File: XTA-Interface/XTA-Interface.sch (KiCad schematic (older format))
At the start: 17 parts, among them CN1 DRIVE 0, CN2 DRIVE 1, CN3 LEDs, CN4 Drive Power, J3 Bus_ISA_8bit, U1 BIOS FLASH, U2 74HCT245, U3 ATF/GAL16V8-15 \"LEFT\", U4 ATF/GAL16V8-15 \"RIGHT\"

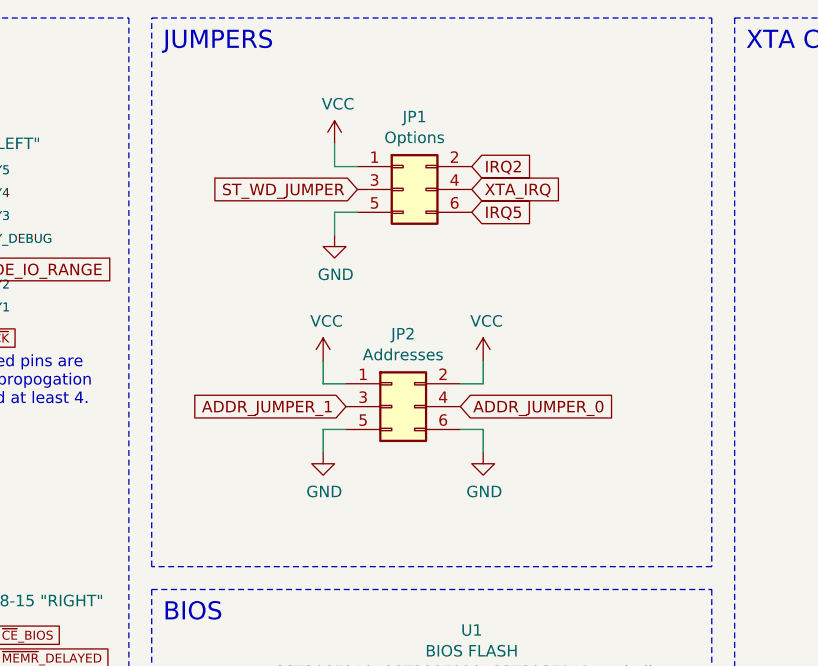
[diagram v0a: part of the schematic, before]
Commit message: Swap positions of A and B jumpers.
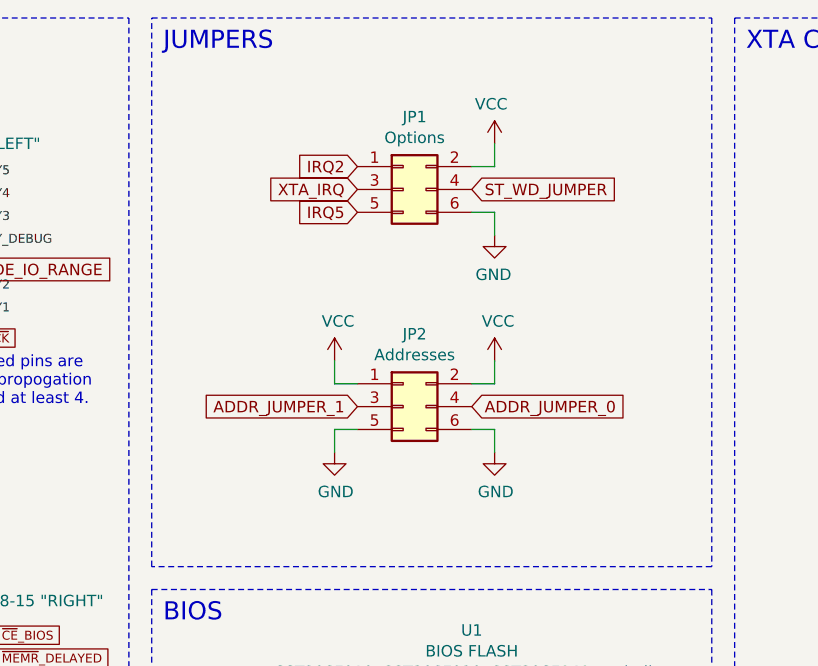
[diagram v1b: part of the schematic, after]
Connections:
- net GND: now also JP1.6 (Pin_6); no longer JP1.5 (Pin_5)
- net IRQ2: now also JP1.1 (Pin_1); no longer JP1.2 (Pin_2)
- net IRQ5: now also JP1.5 (Pin_5); no longer JP1.6 (Pin_6)
- net ST_WD_JUMPER: now also JP1.4 (Pin_4); no longer JP1.3 (Pin_3)
- net VCC: now also JP1.2 (Pin_2); no longer JP1.1 (Pin_1)
- net XTA_IRQ: now also JP1.3 (Pin_3); no longer JP1.4 (Pin_4)
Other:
- moved on the sheet: JP2
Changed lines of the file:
@@
 L power:VCC #PWR0104
 U 1 1 60CA784E
-P 6650 2050
-F 0 "#PWR0104" H 6650 1900 50  0001 C CNN
-F 1 "VCC" H 6665 2223 50  0000 C CNN
-F 2 "" H 6650 2050 50  0001 C CNN
-F 3 "" H 6650 2050 50  0001 C CNN
-	1    6650 2050
+P 6700 2050
+F 0 "#PWR0104" H 6700 1900 50  0001 C CNN
+F 1 "VCC" H 6715 2223 50  0000 C CNN
+F 2 "" H 6700 2050 50  0001 C CNN
+F 3 "" H 6700 2050 50  0001 C CNN
+	1    6700 2050
 	1    0    0    -1
 $EndComp
@@
 L power:VCC #PWR0114
 U 1 1 60CA7D3F
-P 7350 2050
-F 0 "#PWR0114" H 7350 1900 50  0001 C CNN
-F 1 "VCC" H 7365 2223 50  0000 C CNN
-F 2 "" H 7350 2050 50  0001 C CNN
-F 3 "" H 7350 2050 50  0001 C CNN
-	1    7350 2050
+P 7400 2050
+F 0 "#PWR0114" H 7400 1900 50  0001 C CNN
+F 1 "VCC" H 7415 2223 50  0000 C CNN
+F 2 "" H 7400 2050 50  0001 C CNN
+F 3 "" H 7400 2050 50  0001 C CNN
+	1    7400 2050
 	1    0    0    -1
 $EndComp
@@
 L power:GND #PWR0135
 U 1 1 60CA7F88
-P 6650 2450
-F 0 "#PWR0135" H 6650 2200 50  0001 C CNN
-F 1 "GND" H 6655 2277 50  0000 C CNN
-F 2 "" H 6650 2450 50  0001 C CNN
-F 3 "" H 6650 2450 50  0001 C CNN
-	1    6650 2450
+P 6700 2450
+F 0 "#PWR0135" H 6700 2200 50  0001 C CNN
+F 1 "GND" H 6705 2277 50  0000 C CNN
+F 2 "" H 6700 2450 50  0001 C CNN
+F 3 "" H 6700 2450 50  0001 C CNN
+	1    6700 2450
 	1    0    0    -1
 $EndComp
@@
 L power:GND #PWR0136
 U 1 1 60CA8362
-P 7350 2450
-F 0 "#PWR0136" H 7350 2200 50  0001 C CNN
-F 1 "GND" H 7355 2277 50  0000 C CNN
-F 2 "" H 7350 2450 50  0001 C CNN
-F 3 "" H 7350 2450 50  0001 C CNN
-	1    7350 2450
-	1    0    0    -1
-$EndComp
-Wire Wire Line
-	6650 2050 6650 2150
-Wire Wire Line
-	6650 2150 6750 2150
-Wire Wire Line
-	6750 2350 6650 2350
-Wire Wire Line
-	6650 2350 6650 2450
-Wire Wire Line
-	7250 2350 7350 2350
-Wire Wire Line
-	7350 2350 7350 2450
-Wire Wire Line
-	7250 2150 7350 2150
-Wire Wire Line
-	7350 2150 7350 2050
-Text GLabel 7250 2250 2    50   Input ~ 0
+P 7400 2450
+F 0 "#PWR0136" H 7400 2200 50  0001 C CNN
+F 1 "GND" H 7405 2277 50  0000 C CNN
+F 2 "" H 7400 2450 50  0001 C CNN
+F 3 "" H 7400 2450 50  0001 C CNN
+	1    7400 2450
+	1    0    0    -1
+$EndComp
+Wire Wire Line
+	6700 2050 6700 2150
+Wire Wire Line
+	6700 2150 6800 2150
+Wire Wire Line
+	6800 2350 6700 2350
+Wire Wire Line
+	6700 2350 6700 2450
+Wire Wire Line
+	7300 2350 7400 2350
+Wire Wire Line
+	7400 2350 7400 2450
+Wire Wire Line
+	7300 2150 7400 2150
+Wire Wire Line
+	7400 2150 7400 2050
+Text GLabel 7300 2250 2    50   Input ~ 0
 ADDR_JUMPER_0
 $Comp
 L power:VCC #PWR0137
 U 1 1 60CBC833
-P 6700 1100
-F 0 "#PWR0137" H 6700 950 50  0001 C CNN
-F 1 "VCC" H 6715 1273 50  0000 C CNN
-F 2 "" H 6700 1100 50  0001 C CNN
-F 3 "" H 6700 1100 50  0001 C CNN
-	1    6700 1100
-	1    0    0    -1
+P 7400 1100
+F 0 "#PWR0137" H 7400 950 50  0001 C CNN
+F 1 "VCC" H 7415 1273 50  0000 C CNN
+F 2 "" H 7400 1100 50  0001 C CNN
+F 3 "" H 7400 1100 50  0001 C CNN
+	1    7400 1100
+	-1   0    0    -1
 $EndComp
 $Comp
 L power:GND #PWR0138
 U 1 1 60CBC847
-P 6700 1500
-F 0 "#PWR0138" H 6700 1250 50  0001 C CNN
-F 1 "GND" H 6705 1327 50  0000 C CNN
-F 2 "" H 6700 1500 50  0001 C CNN
-F 3 "" H 6700 1500 50  0001 C CNN
-	1    6700 1500
-	1    0    0    -1
-$EndComp
-Wire Wire Line
-	6700 1100 6700 1200
-Wire Wire Line
-	6700 1200 6800 1200
-Wire Wire Line
-	6800 1400 6700 1400
-Wire Wire Line
-	6700 1400 6700 1500
+P 7400 1500
+F 0 "#PWR0138" H 7400 1250 50  0001 C CNN
+F 1 "GND" H 7405 1327 50  0000 C CNN
+F 2 "" H 7400 1500 50  0001 C CNN
+F 3 "" H 7400 1500 50  0001 C CNN
+	1    7400 1500
+	-1   0    0    -1
+$EndComp
+Wire Wire Line
+	7400 1100 7400 1200
+Wire Wire Line
+	7400 1200 7300 1200
+Wire Wire Line
+	7300 1400 7400 1400
+Wire Wire Line
+	7400 1400 7400 1500
 Text GLabel 9450 2850 0    39   Input ~ 0
 ~DRV_ACTIVE
@@
 Text GLabel 9450 3900 0    50   Input ~ 0
 D7
-Text GLabel 6750 2250 0    50   Input ~ 0
+Text GLabel 6800 2250 0    50   Input ~ 0
 ADDR_JUMPER_1
+Text GLabel 7300 1300 2    50   Input ~ 0
+ST_WD_JUMPER
 Text GLabel 6800 1300 0    50   Input ~ 0
-ST_WD_JUMPER
-Text GLabel 7300 1300 2    50   Input ~ 0
 XTA_IRQ
 Text GLabel 1200 3200 0    50   Input ~ 0
@@
 Text GLabel 950  1300 0    50   Input ~ 0
 IRQ2
-Text GLabel 7300 1200 2    50   Input ~ 0
+Text GLabel 6800 1200 0    50   Input ~ 0
 IRQ2
-Text GLabel 7300 1400 2    50   Input ~ 0
+Text GLabel 6800 1400 0    50   Input ~ 0
 IRQ5
 $Comp
@@
 L Connector_Generic:Conn_02x03_Odd_Even JP2
 U 1 1 60CA67F2
-P 6950 2250
-F 0 "JP2" H 7000 2567 50  0000 C CNN
-F 1 "Addresses" H 7000 2476 50  0000 C CNN
-F 2 "Connector_PinHeader_2.54mm:PinHeader_2x03_P2.54mm_Vertical" H 6950 2250 50  0001 C CNN
-F 3 "~" H 6950 2250 50  0001 C CNN
-	1    6950 2250
-	1    0    0    -1
-$EndComp
+P 7000 2250
+F 0 "JP2" H 7050 2567 50  0000 C CNN
+F 1 "Addresses" H 7050 2476 50  0000 C CNN
+F 2 "Connector_PinHeader_2.54mm:PinHeader_2x03_P2.54mm_Vertical" H 7000 2250 50  0001 C CNN
+F 3 "~" H 7000 2250 50  0001 C CNN
+	1    7000 2250
+	1    0    0    -1
+$EndComp

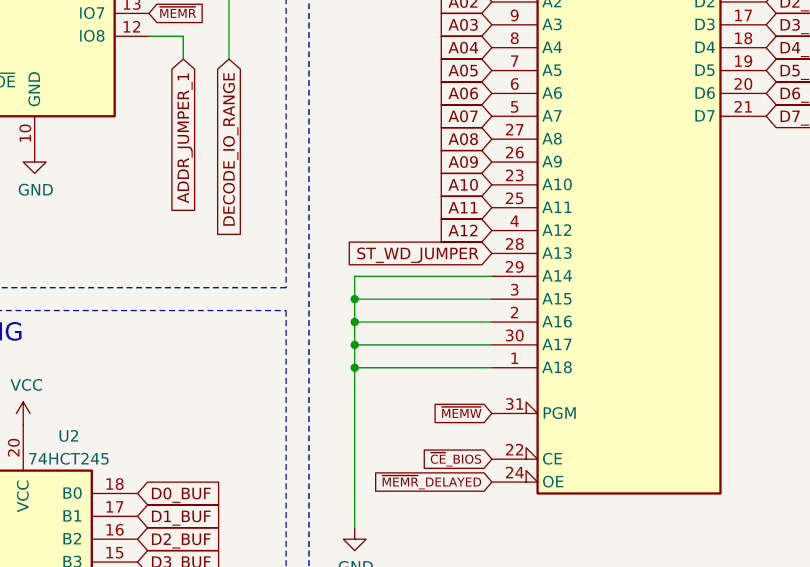
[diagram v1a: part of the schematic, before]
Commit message: XTA-Interface: Change how ST_WD_JUMPER is connected to flash ROM. Layout still needs to be updated.
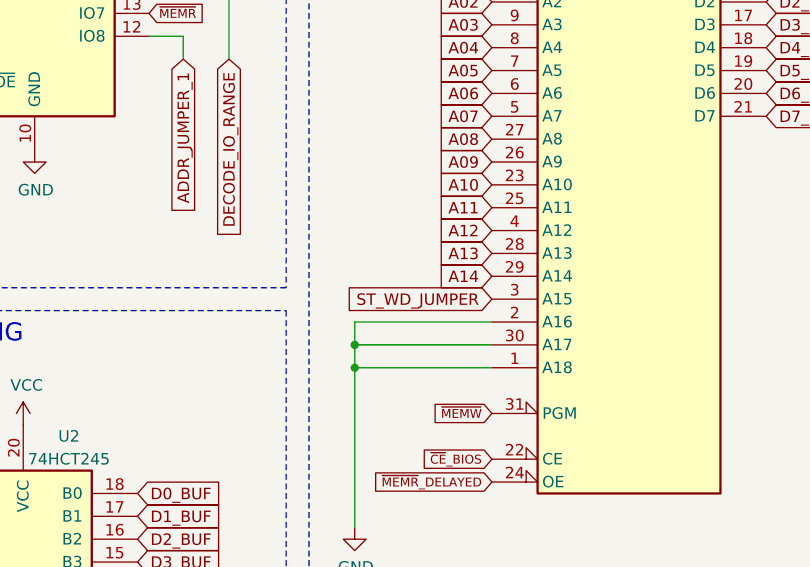
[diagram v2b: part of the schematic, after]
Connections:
- net A13: now also U1.28 (A13)
- net A14: now also U1.29 (A14)
- net GND: no longer U1.29 (A14), U1.3 (A15)
- net ST_WD_JUMPER: now also U1.3 (A15); no longer U1.28 (A13)
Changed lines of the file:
@@
 Wire Wire Line
 	6100 5300 6100 5400
-Text GLabel 6700 4900 0    50   Input ~ 0
-ST_WD_JUMPER
 $Comp
 L Device:C C1
@@
 Wire Notes Line
 	5900 6450 8350 6450
-Wire Wire Line
-	6700 5000 6100 5000
-Wire Wire Line
-	6100 5000 6100 5100
 Connection ~ 6100 5300
 Wire Wire Line
-	6700 5100 6100 5100
-Connection ~ 6100 5100
-Wire Wire Line
-	6100 5100 6100 5200
-Wire Wire Line
 	6700 5200 6100 5200
-Connection ~ 6100 5200
 Wire Wire Line
 	6100 5200 6100 5300
@@
 Wire Wire Line
 	5550 3750 5200 3750
+Text GLabel 6700 5100 0    50   Input ~ 0
+ST_WD_JUMPER
+Text GLabel 6700 4900 0    50   Input ~ 0
+A13
+Text GLabel 6700 5000 0    50   Input ~ 0
+A14
 $EndSCHEMATC

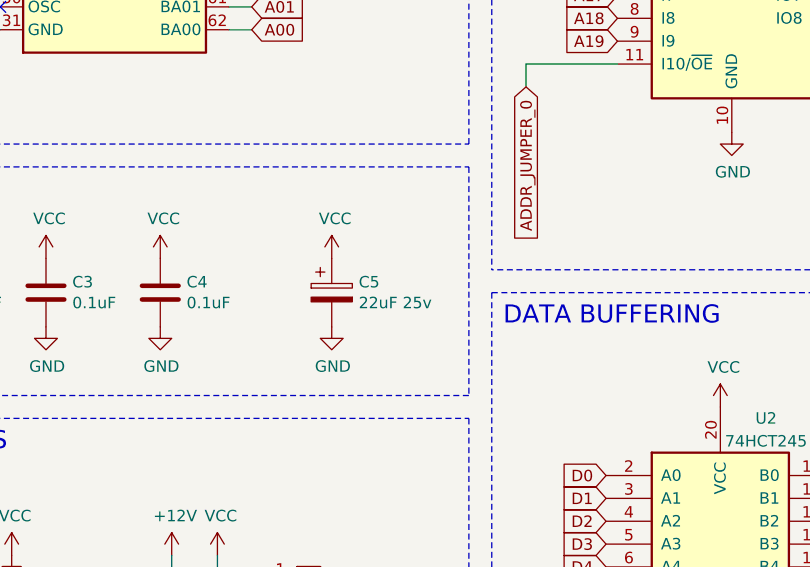
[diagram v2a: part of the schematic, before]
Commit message: XTA-Interface: Change tantalum capacitor value text.
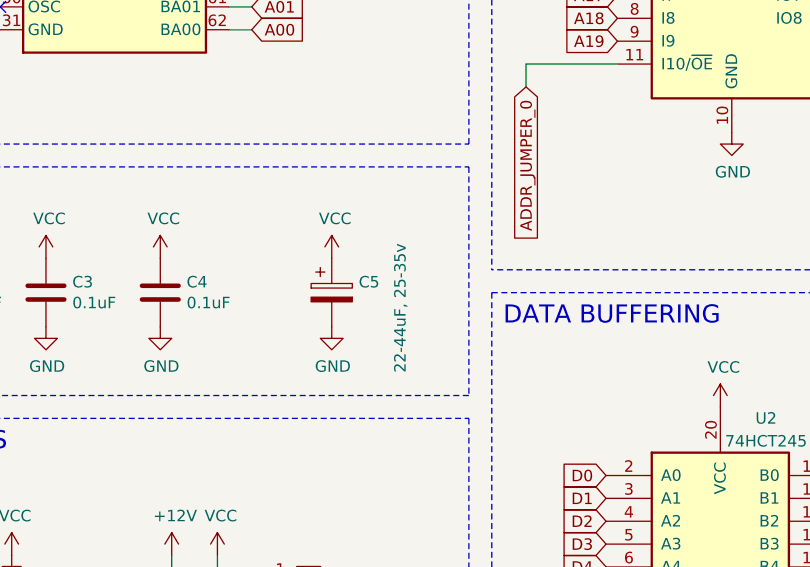
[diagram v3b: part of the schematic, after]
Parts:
- C5: value 22uF 25v -> 22-44uF, 25-35v
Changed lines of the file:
@@
 P 2950 5150
 F 0 "C5" H 3068 5196 50  0000 L CNN
-F 1 "22uF 25v" H 3068 5105 50  0000 L CNN
+F 1 "22-44uF, 25-35v" V 3250 4800 50  0000 L CNN
 F 2 "Capacitor_Tantalum_SMD:CP_EIA-3528-15_AVX-H" H 2988 5000 50  0001 C CNN
 F 3 "~" H 2950 5150 50  0001 C CNN
